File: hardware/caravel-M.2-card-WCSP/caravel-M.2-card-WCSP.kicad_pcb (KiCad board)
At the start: 4 copper layers, 22 x 22 mm, 11 parts, among them J1 MICROMOD-2222-Generic, T1 Logo, T2 Logo, U1 Caravel

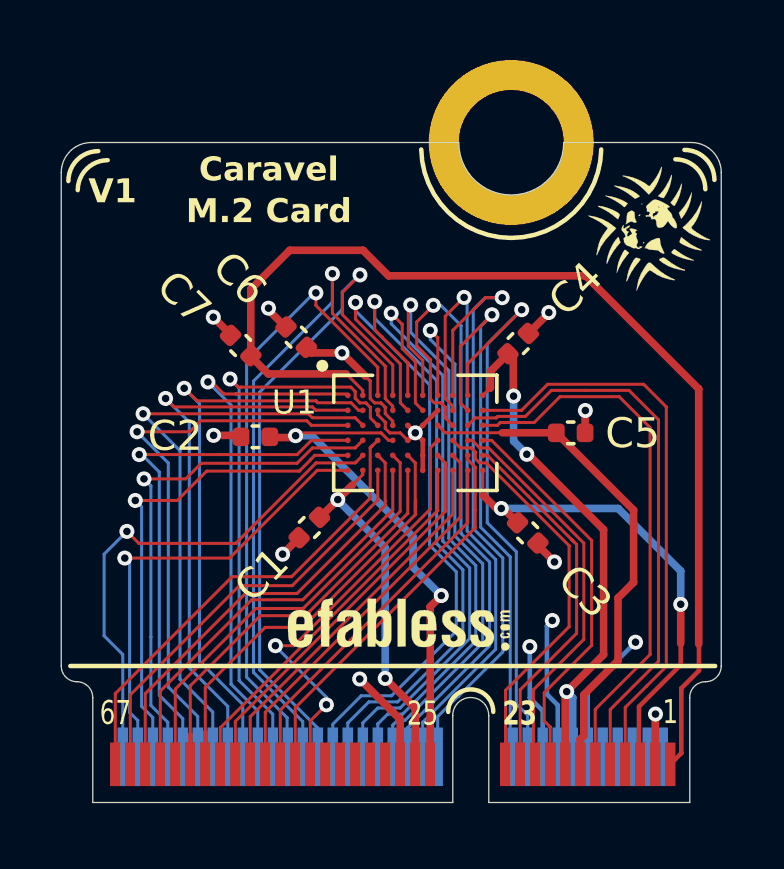
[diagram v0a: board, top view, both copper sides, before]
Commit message: update Caravel M.2 card PCB + add large via for each power domain to ease monitoring them
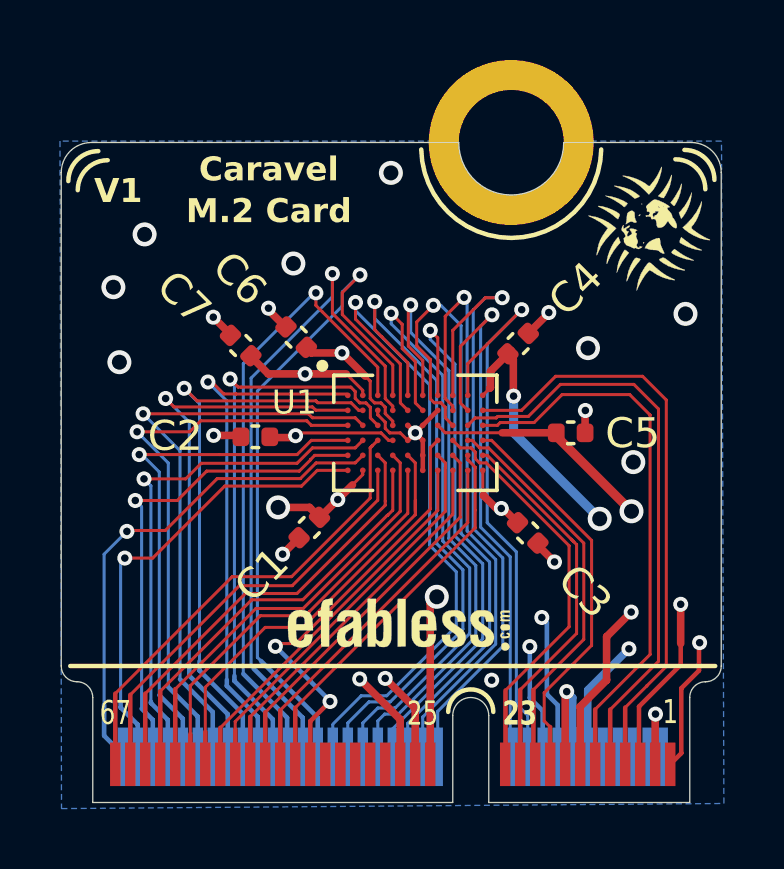
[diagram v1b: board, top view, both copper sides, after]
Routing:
- net vdda: track 16.0 -> 20.3 mm, vias 2 -> 3
- net vccd1: track 12.1 -> 13.6 mm, vias 2 -> 3
- net vdda1: track 17.7 -> 18.5 mm
- net GND: track 22.4 -> 22.1 mm, vias 11 -> 17
- net vccd2: track 36.9 -> 36.7 mm, vias 0 -> 3
- net vddio: track 10.9 -> 11.0 mm, vias 3 -> 4
- net vdda2: track 16.9 -> 17.0 mm, vias 0 -> 2
- added copper zone on B.Cu, net GND

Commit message: update Caravel M.2 card PCBs - remove copper fill at the card edge to avoid shorts when the card is inserted in the M.2 connector
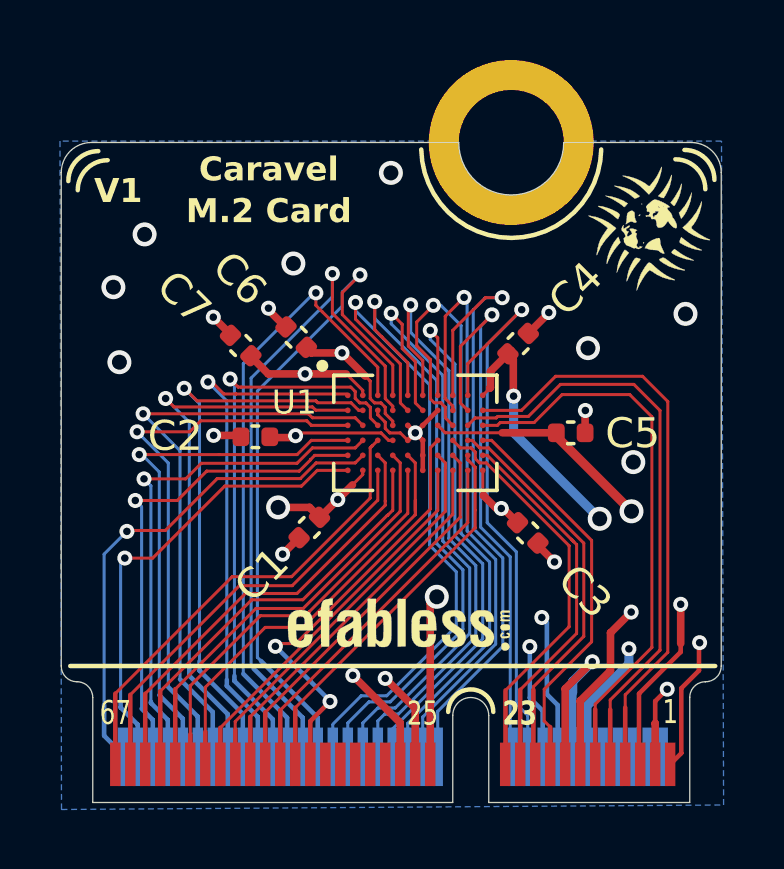
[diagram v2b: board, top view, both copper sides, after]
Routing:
- net vccd: track 19.7 -> 20.9 mm
- net vddio: track 11.0 -> 12.0 mm
- net GND: track 22.1 -> 22.3 mm, vias 17 -> 16
